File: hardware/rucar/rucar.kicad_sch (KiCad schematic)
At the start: 26 parts

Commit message: fix design
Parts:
- M?: value 右后轮电机 -> 左后轮电机
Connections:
- net at U?. (VDD): now also D?.2 (A), D?.2 (A), D?.2 (A), D?.2 (A); no longer U?. (Sig)
- net at U?. (~{RECLED}): now also U?. (VCC); no longer U?. (Sig)
- new net: U?. (Sig), U?. (VDD) (x2)
- new net: U?. (Sig), U?. (~{RECLED}) (x2)
- new net: U?. (VCC), U?. (~{RECLED})
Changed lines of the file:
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@@
       (effects (font (size 1.27 1.27)) (justify left) hide)
     )
-    (property "Value" "右后轮电机" (id 1) (at 179.07 85.09 0)
+    (property "Value" "左后轮电机" (id 1) (at 179.07 85.09 0)
       (effects (font (size 1.27 1.27)) (justify left))
     )
@@
     )
     (path "/ce4d2b31-1cfb-49cf-ae5a-fb9edfcff7ff"
-      (reference "M?") (unit 1) (value "右后轮电机") (footprint "")
+      (reference "M?") (unit 1) (value "左后轮电机") (footprint "")
     )
     (path "/215e4f7e-cb3d-4fdc-8eae-7a3d229e2f0b"

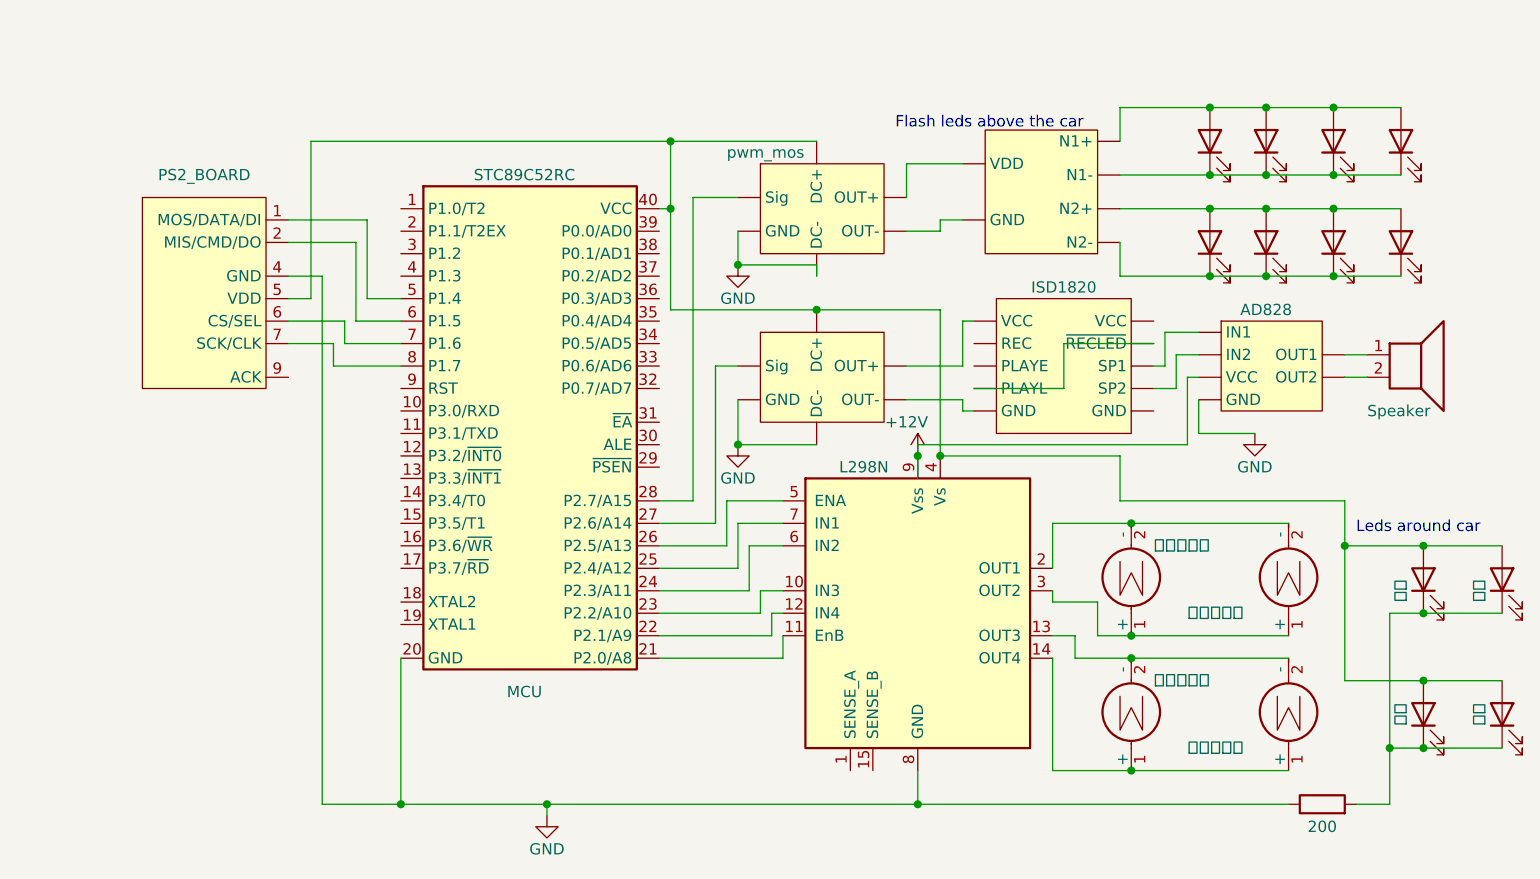
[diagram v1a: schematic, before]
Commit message: v3-change to gimbal
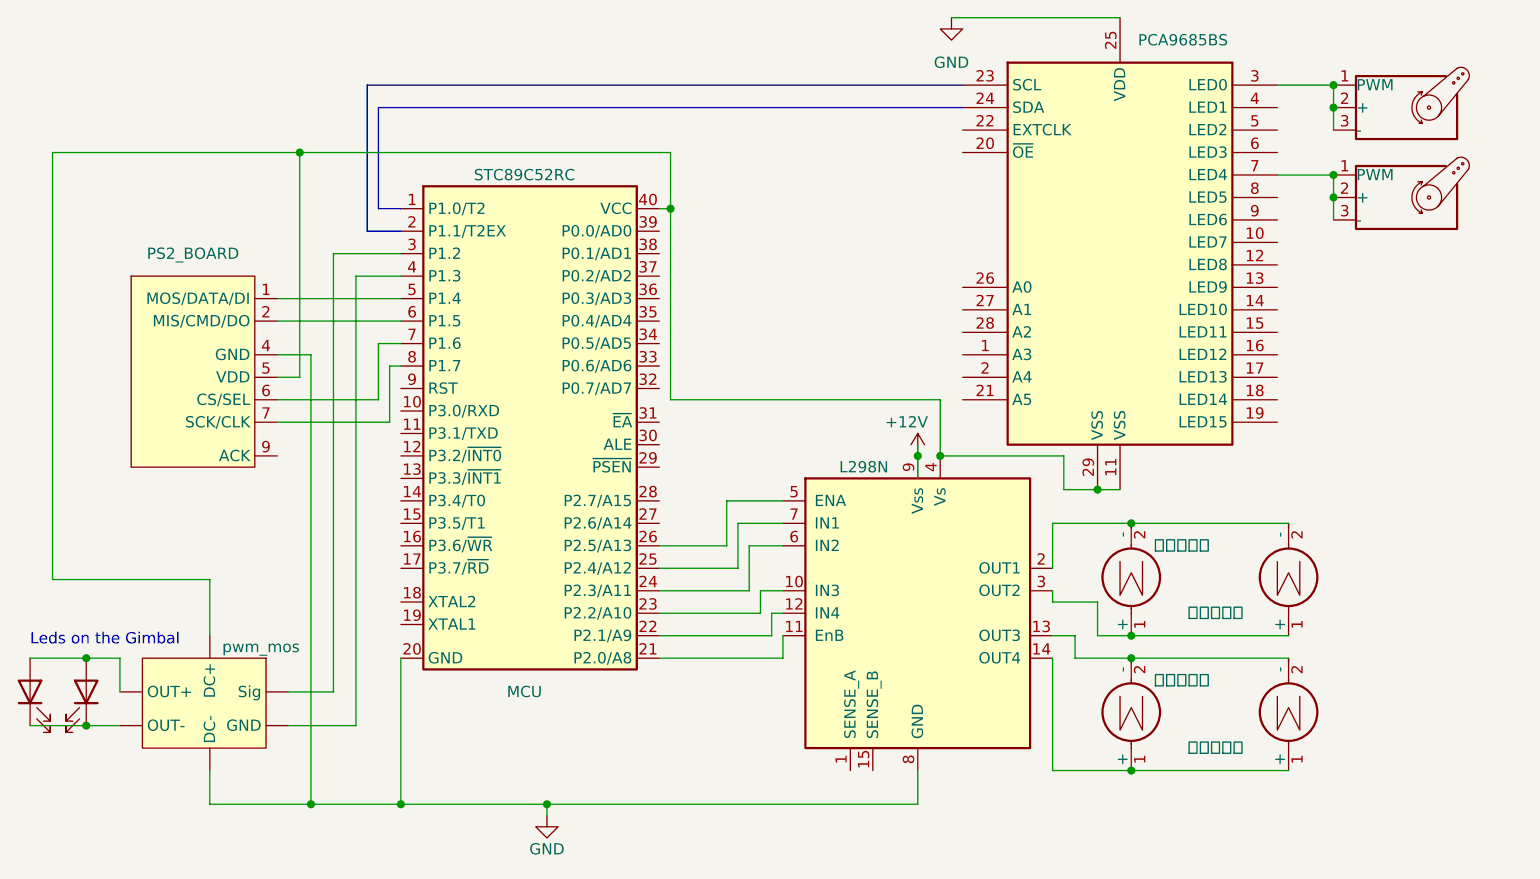
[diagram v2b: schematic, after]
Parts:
- removed D: 右前, symbol Device:LED
- removed D: 左前, symbol Device:LED
- removed D: 左后, symbol Device:LED
- removed D: 右后, symbol Device:LED
- removed D? (x6): LED, symbol Device:LED
- removed LS?: Speaker, symbol Device:Speaker
- removed R?: 200, symbol Device:R
- removed U?: pwm_mos, symbol Power_Management:pwm_mos
- removed U?: ISD1820, symbol Audio:ISD1820
- removed U?: AD828, symbol Audio:AD828
- removed U?: self_define_led_driver, symbol Driver_LED:self_define_led_driver
- added M? (x2): Motor_Servo, symbol Motor:Motor_Servo
- added U?: PCA9685BS, Package_DFN_QFN:QFN-28-1EP_6x6mm_P0.65mm_EP4.25x4.25mm, symbol Driver_LED:PCA9685BS
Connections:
- net GND: now also U?.25 (VDD)
- net at D?.1 (K): now also D?.1 (K), U?. (Sig)
- net at D?.2 (A): now also D?.2 (A), U?. (Sig)
- net at MCU.28 (P2.7/A15): no longer U?. (Sig)
- net at MCU.3 (P1.2): now also U?. (Sig)
- net at MCU.4 (P1.3): now also U?. (Sig)
- net at MCU.40 (VCC), U?. (Sig), U?.4 (Vs)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: now also U?.11 (VSS), U?.29 (VSS)
- new net: M?.1 (PWM), M?.2 (+), M?.3 (-), U?.3 (LED0)
- new net: M?.1 (PWM), M?.2 (+), M?.3 (-), U?.7 (LED4)
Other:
- note added: "Leds on the Gimbal"
- note removed: "Flash leds above the car"
- note removed: "Leds around car"
